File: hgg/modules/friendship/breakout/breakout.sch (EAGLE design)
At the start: 7 parts, among them IC1 MAX481CSA, IC2 MAX481CSA

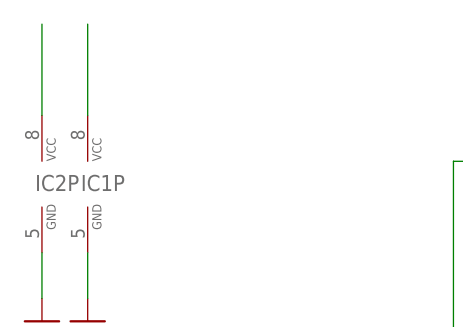
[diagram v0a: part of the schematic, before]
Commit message: max485 now running @ 5V vcc
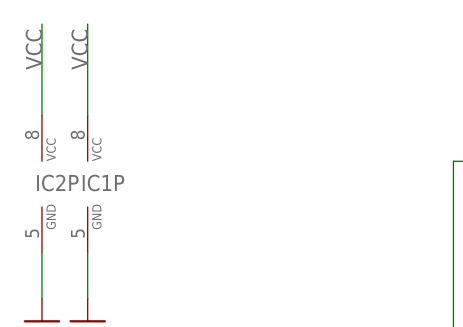
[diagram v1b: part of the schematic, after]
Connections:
- removed net N$18: JP1.3, U$1.+5V_A
- new net 3V3: JP1.7, U$1.+3V3_A
- net VCC: now also JP1.3, U$1.+5V_A; no longer JP1.7, U$1.+3V3_A
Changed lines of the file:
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@@
 <pinref part="IC1" gate="P" pin="VCC"/>
 <wire x1="-76.2" y1="96.52" x2="-76.2" y2="106.68" width="0.1524" layer="91"/>
+<label x="-76.2" y="101.6" size="1.778" layer="95" rot="R90"/>
 </segment>
 <segment>
 <pinref part="IC2" gate="P" pin="VCC"/>
 <wire x1="-81.28" y1="96.52" x2="-81.28" y2="106.68" width="0.1524" layer="91"/>
+<label x="-81.28" y="101.6" size="1.778" layer="95" rot="R90"/>
 </segment>
 <segment>
-<pinref part="U$1" gate="G$1" pin="+3V3_A"/>
-<wire x1="50.8" y1="68.58" x2="50.8" y2="71.12" width="0.1524" layer="91"/>
-<pinref part="JP1" gate="A" pin="7"/>
-<wire x1="50.8" y1="71.12" x2="35.56" y2="71.12" width="0.1524" layer="91"/>
+<pinref part="U$1" gate="G$1" pin="+5V_A"/>
+<wire x1="50.8" y1="63.5" x2="40.64" y2="63.5" width="0.1524" layer="91"/>
+<wire x1="40.64" y1="63.5" x2="40.64" y2="60.96" width="0.1524" layer="91"/>
+<pinref part="JP1" gate="A" pin="3"/>
+<wire x1="40.64" y1="60.96" x2="35.56" y2="60.96" width="0.1524" layer="91"/>
 </segment>
 </net>
@@
 <pinref part="JP1" gate="A" pin="5"/>
 <wire x1="35.56" y1="66.04" x2="43.18" y2="66.04" width="0.1524" layer="91"/>
-</segment>
-</net>
-<net name="N$18" class="0">
-<segment>
-<pinref part="U$1" gate="G$1" pin="+5V_A"/>
-<wire x1="50.8" y1="63.5" x2="40.64" y2="63.5" width="0.1524" layer="91"/>
-<wire x1="40.64" y1="63.5" x2="40.64" y2="60.96" width="0.1524" layer="91"/>
-<pinref part="JP1" gate="A" pin="3"/>
-<wire x1="40.64" y1="60.96" x2="35.56" y2="60.96" width="0.1524" layer="91"/>
 </segment>
 </net>
@@
 </segment>
 </net>
+<net name="3V3" class="0">
+<segment>
+<pinref part="U$1" gate="G$1" pin="+3V3_A"/>
+<wire x1="50.8" y1="68.58" x2="50.8" y2="71.12" width="0.1524" layer="91"/>
+<pinref part="JP1" gate="A" pin="7"/>
+<wire x1="50.8" y1="71.12" x2="35.56" y2="71.12" width="0.1524" layer="91"/>
+</segment>
+</net>

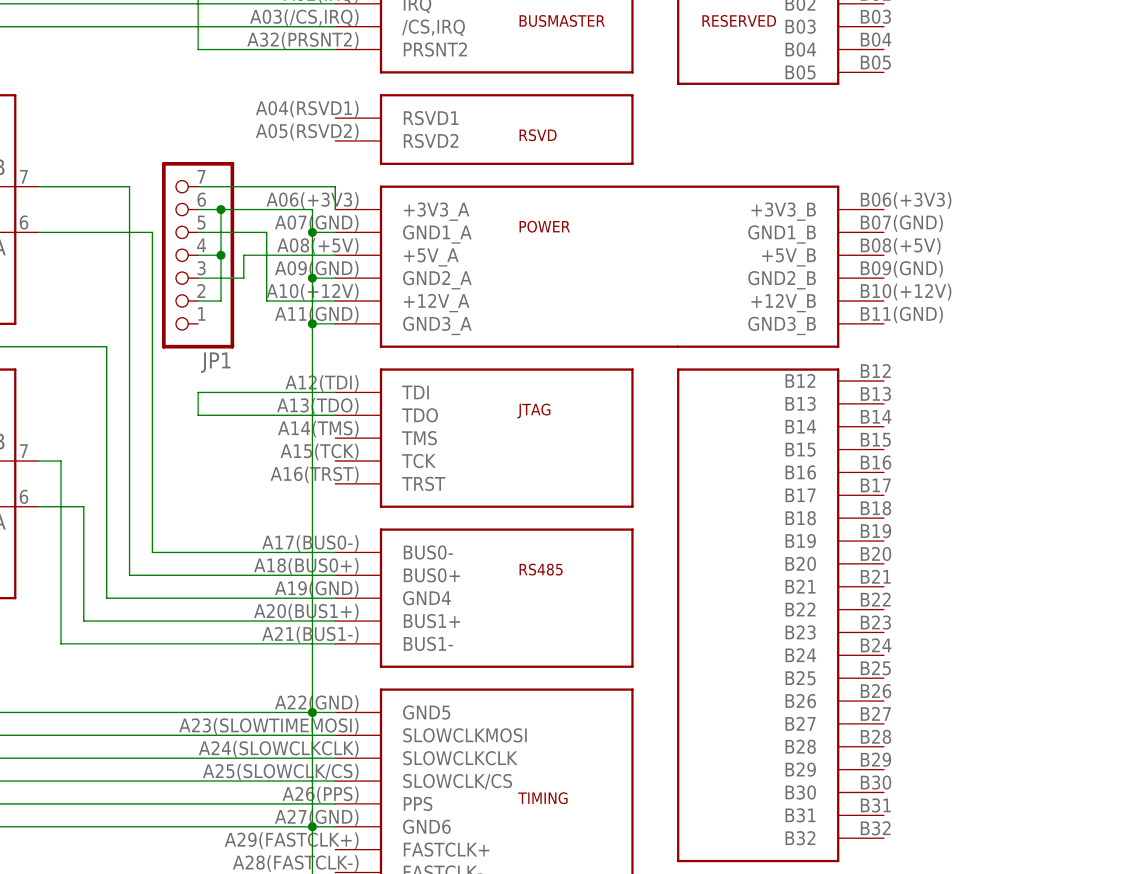
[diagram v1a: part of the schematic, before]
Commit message: swapped sides of the pcb
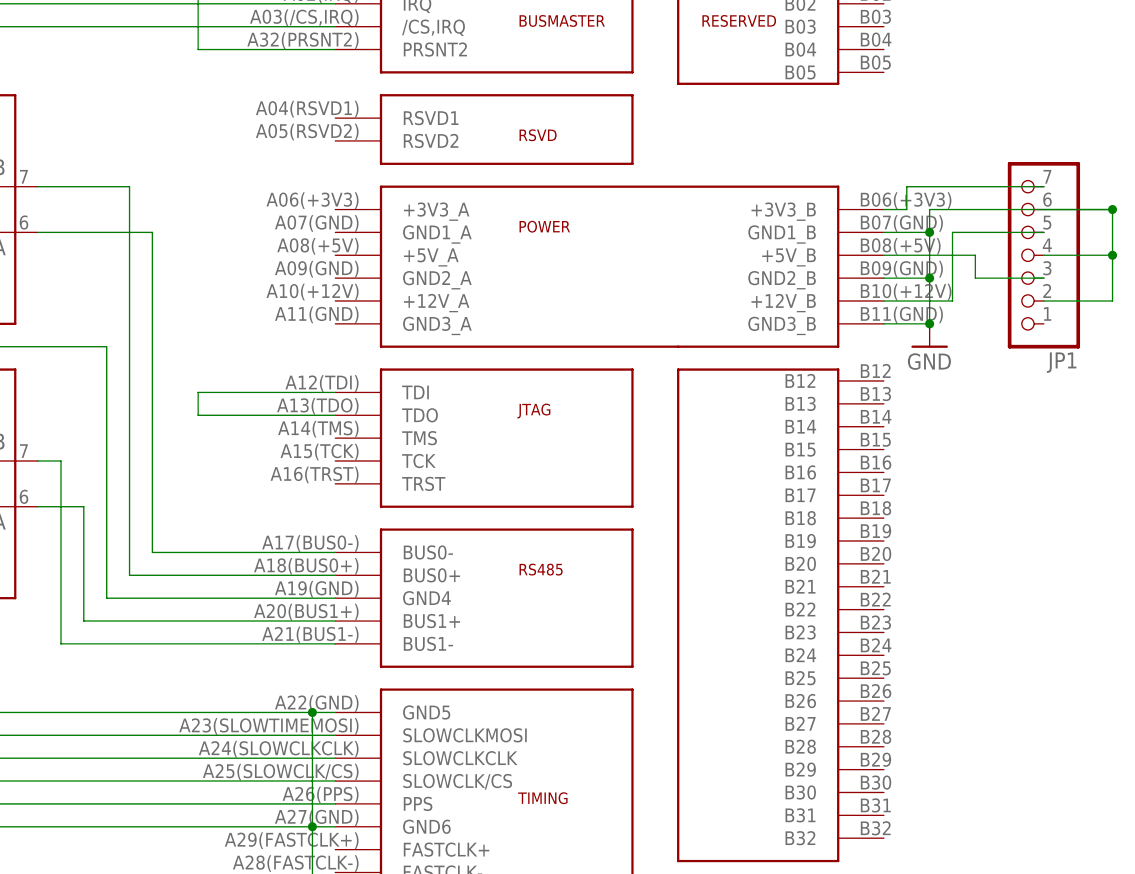
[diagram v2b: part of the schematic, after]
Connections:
- removed net N$13: JP1.5, U$1.+12V_A
- new net 12V: JP1.5, U$1.+12V_B
- net 3V3: now also U$1.+3V3_B; no longer U$1.+3V3_A
- net GND: now also U$1.GND1_B, U$1.GND2_B, U$1.GND3_B; no longer U$1.GND1_A, U$1.GND2_A, U$1.GND3_A
- net VCC: no longer U$1.+5V_A
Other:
- moved on the sheet: JP1
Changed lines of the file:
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@@
 <part name="JP3" library="pinhead" deviceset="PINHD-1X10" device=""/>
 <part name="JP4" library="pinhead" deviceset="PINHD-2X5" device=""/>
+<part name="GND4" library="supply1" deviceset="GND" device=""/>
 </parts>
 <sheets>
@@
 <instance part="IC1" gate="G$1" x="5.08" y="38.1"/>
 <instance part="IC2" gate="G$1" x="5.08" y="68.58"/>
-<instance part="JP1" gate="A" x="33.02" y="63.5" rot="R180"/>
+<instance part="JP1" gate="A" x="127" y="63.5" rot="R180"/>
 <instance part="JP2" gate="A" x="-50.8" y="40.64" rot="R180"/>
 <instance part="IC2" gate="P" x="-81.28" y="88.9"/>
@@
 <instance part="JP3" gate="A" x="40.64" y="-50.8" rot="R180"/>
 <instance part="JP4" gate="A" x="73.66" y="-43.18"/>
+<instance part="GND4" gate="1" x="116.84" y="53.34"/>
 </instances>
 <busses>
@@
 <wire x1="-30.48" y1="25.4" x2="-48.26" y2="25.4" width="0.1524" layer="91"/>
 <junction x="48.26" y="0"/>
-<pinref part="U$1" gate="G$1" pin="GND1_A"/>
-<wire x1="48.26" y1="66.04" x2="50.8" y2="66.04" width="0.1524" layer="91"/>
-<wire x1="48.26" y1="66.04" x2="48.26" y2="60.96" width="0.1524" layer="91"/>
 <pinref part="JP2" gate="A" pin="2"/>
 <pinref part="JP2" gate="A" pin="7"/>
-<pinref part="U$1" gate="G$1" pin="GND2_A"/>
-<wire x1="48.26" y1="60.96" x2="48.26" y2="55.88" width="0.1524" layer="91"/>
-<wire x1="48.26" y1="55.88" x2="48.26" y2="12.7" width="0.1524" layer="91"/>
-<wire x1="50.8" y1="60.96" x2="48.26" y2="60.96" width="0.1524" layer="91"/>
-<junction x="48.26" y="60.96"/>
-<pinref part="U$1" gate="G$1" pin="GND3_A"/>
-<wire x1="50.8" y1="55.88" x2="48.26" y2="55.88" width="0.1524" layer="91"/>
-<junction x="48.26" y="55.88"/>
-<wire x1="48.26" y1="66.04" x2="48.26" y2="68.58" width="0.1524" layer="91"/>
-<junction x="48.26" y="66.04"/>
-<pinref part="JP1" gate="A" pin="2"/>
-<wire x1="35.56" y1="58.42" x2="38.1" y2="58.42" width="0.1524" layer="91"/>
-<wire x1="38.1" y1="58.42" x2="38.1" y2="63.5" width="0.1524" layer="91"/>
-<pinref part="JP1" gate="A" pin="4"/>
-<wire x1="38.1" y1="63.5" x2="35.56" y2="63.5" width="0.1524" layer="91"/>
-<wire x1="38.1" y1="63.5" x2="38.1" y2="68.58" width="0.1524" layer="91"/>
-<junction x="38.1" y="63.5"/>
-<pinref part="JP1" gate="A" pin="6"/>
-<wire x1="38.1" y1="68.58" x2="35.56" y2="68.58" width="0.1524" layer="91"/>
-<wire x1="38.1" y1="68.58" x2="48.26" y2="68.58" width="0.1524" layer="91"/>
-<junction x="38.1" y="68.58"/>
 </segment>
 <segment>
@@
 <pinref part="GND3" gate="1" pin="GND"/>
 <wire x1="-76.2" y1="76.2" x2="-76.2" y2="81.28" width="0.1524" layer="91"/>
+</segment>
+<segment>
+<pinref part="JP1" gate="A" pin="6"/>
+<pinref part="JP1" gate="A" pin="4"/>
+<pinref part="JP1" gate="A" pin="2"/>
+<wire x1="129.54" y1="58.42" x2="137.16" y2="58.42" width="0.1524" layer="91"/>
+<wire x1="137.16" y1="58.42" x2="137.16" y2="63.5" width="0.1524" layer="91"/>
+<wire x1="137.16" y1="63.5" x2="129.54" y2="63.5" width="0.1524" layer="91"/>
+<junction x="137.16" y="63.5"/>
+<wire x1="137.16" y1="63.5" x2="137.16" y2="68.58" width="0.1524" layer="91"/>
+<wire x1="137.16" y1="68.58" x2="129.54" y2="68.58" width="0.1524" layer="91"/>
+<junction x="137.16" y="68.58"/>
+<wire x1="137.16" y1="68.58" x2="116.84" y2="68.58" width="0.1524" layer="91"/>
+<wire x1="116.84" y1="68.58" x2="116.84" y2="66.04" width="0.1524" layer="91"/>
+<pinref part="U$1" gate="G$1" pin="GND1_B"/>
+<wire x1="116.84" y1="66.04" x2="111.76" y2="66.04" width="0.1524" layer="91"/>
+<wire x1="116.84" y1="66.04" x2="116.84" y2="60.96" width="0.1524" layer="91"/>
+<junction x="116.84" y="66.04"/>
+<pinref part="U$1" gate="G$1" pin="GND2_B"/>
+<wire x1="116.84" y1="60.96" x2="111.76" y2="60.96" width="0.1524" layer="91"/>
+<wire x1="116.84" y1="60.96" x2="116.84" y2="55.88" width="0.1524" layer="91"/>
+<junction x="116.84" y="60.96"/>
+<pinref part="U$1" gate="G$1" pin="GND3_B"/>
+<wire x1="116.84" y1="55.88" x2="111.76" y2="55.88" width="0.1524" layer="91"/>
+<pinref part="GND4" gate="1" pin="GND"/>
+<junction x="116.84" y="55.88"/>
 </segment>
 </net>
@@
 </segment>
 <segment>
-<pinref part="U$1" gate="G$1" pin="+5V_A"/>
-<wire x1="50.8" y1="63.5" x2="40.64" y2="63.5" width="0.1524" layer="91"/>
-<wire x1="40.64" y1="63.5" x2="40.64" y2="60.96" width="0.1524" layer="91"/>
+<wire x1="111.76" y1="63.5" x2="121.92" y2="63.5" width="0.1524" layer="91"/>
+<wire x1="121.92" y1="63.5" x2="121.92" y2="60.96" width="0.1524" layer="91"/>
 <pinref part="JP1" gate="A" pin="3"/>
-<wire x1="40.64" y1="60.96" x2="35.56" y2="60.96" width="0.1524" layer="91"/>
+<wire x1="121.92" y1="60.96" x2="129.54" y2="60.96" width="0.1524" layer="91"/>
 </segment>
 </net>
@@
 </segment>
 </net>
-<net name="N$13" class="0">
-<segment>
-<pinref part="U$1" gate="G$1" pin="+12V_A"/>
-<wire x1="50.8" y1="58.42" x2="43.18" y2="58.42" width="0.1524" layer="91"/>
-<wire x1="43.18" y1="58.42" x2="43.18" y2="66.04" width="0.1524" layer="91"/>
+<net name="12V" class="0">
+<segment>
+<wire x1="119.38" y1="58.42" x2="119.38" y2="66.04" width="0.1524" layer="91"/>
 <pinref part="JP1" gate="A" pin="5"/>
-<wire x1="35.56" y1="66.04" x2="43.18" y2="66.04" width="0.1524" layer="91"/>
+<wire x1="129.54" y1="66.04" x2="119.38" y2="66.04" width="0.1524" layer="91"/>
+<pinref part="U$1" gate="G$1" pin="+12V_B"/>
+<wire x1="119.38" y1="58.42" x2="111.76" y2="58.42" width="0.1524" layer="91"/>
 </segment>
 </net>
@@
 <net name="3V3" class="0">
 <segment>
-<pinref part="U$1" gate="G$1" pin="+3V3_A"/>
-<wire x1="50.8" y1="68.58" x2="50.8" y2="71.12" width="0.1524" layer="91"/>
 <pinref part="JP1" gate="A" pin="7"/>
-<wire x1="50.8" y1="71.12" x2="35.56" y2="71.12" width="0.1524" layer="91"/>
-</segment>
-</net>
+<wire x1="114.3" y1="71.12" x2="129.54" y2="71.12" width="0.1524" layer="91"/>
+<pinref part="U$1" gate="G$1" pin="+3V3_B"/>
+<wire x1="111.76" y1="68.58" x2="114.3" y2="68.58" width="0.1524" layer="91"/>
+<wire x1="114.3" y1="68.58" x2="114.3" y2="71.12" width="0.1524" layer="91"/>
+</segment>
+</net>

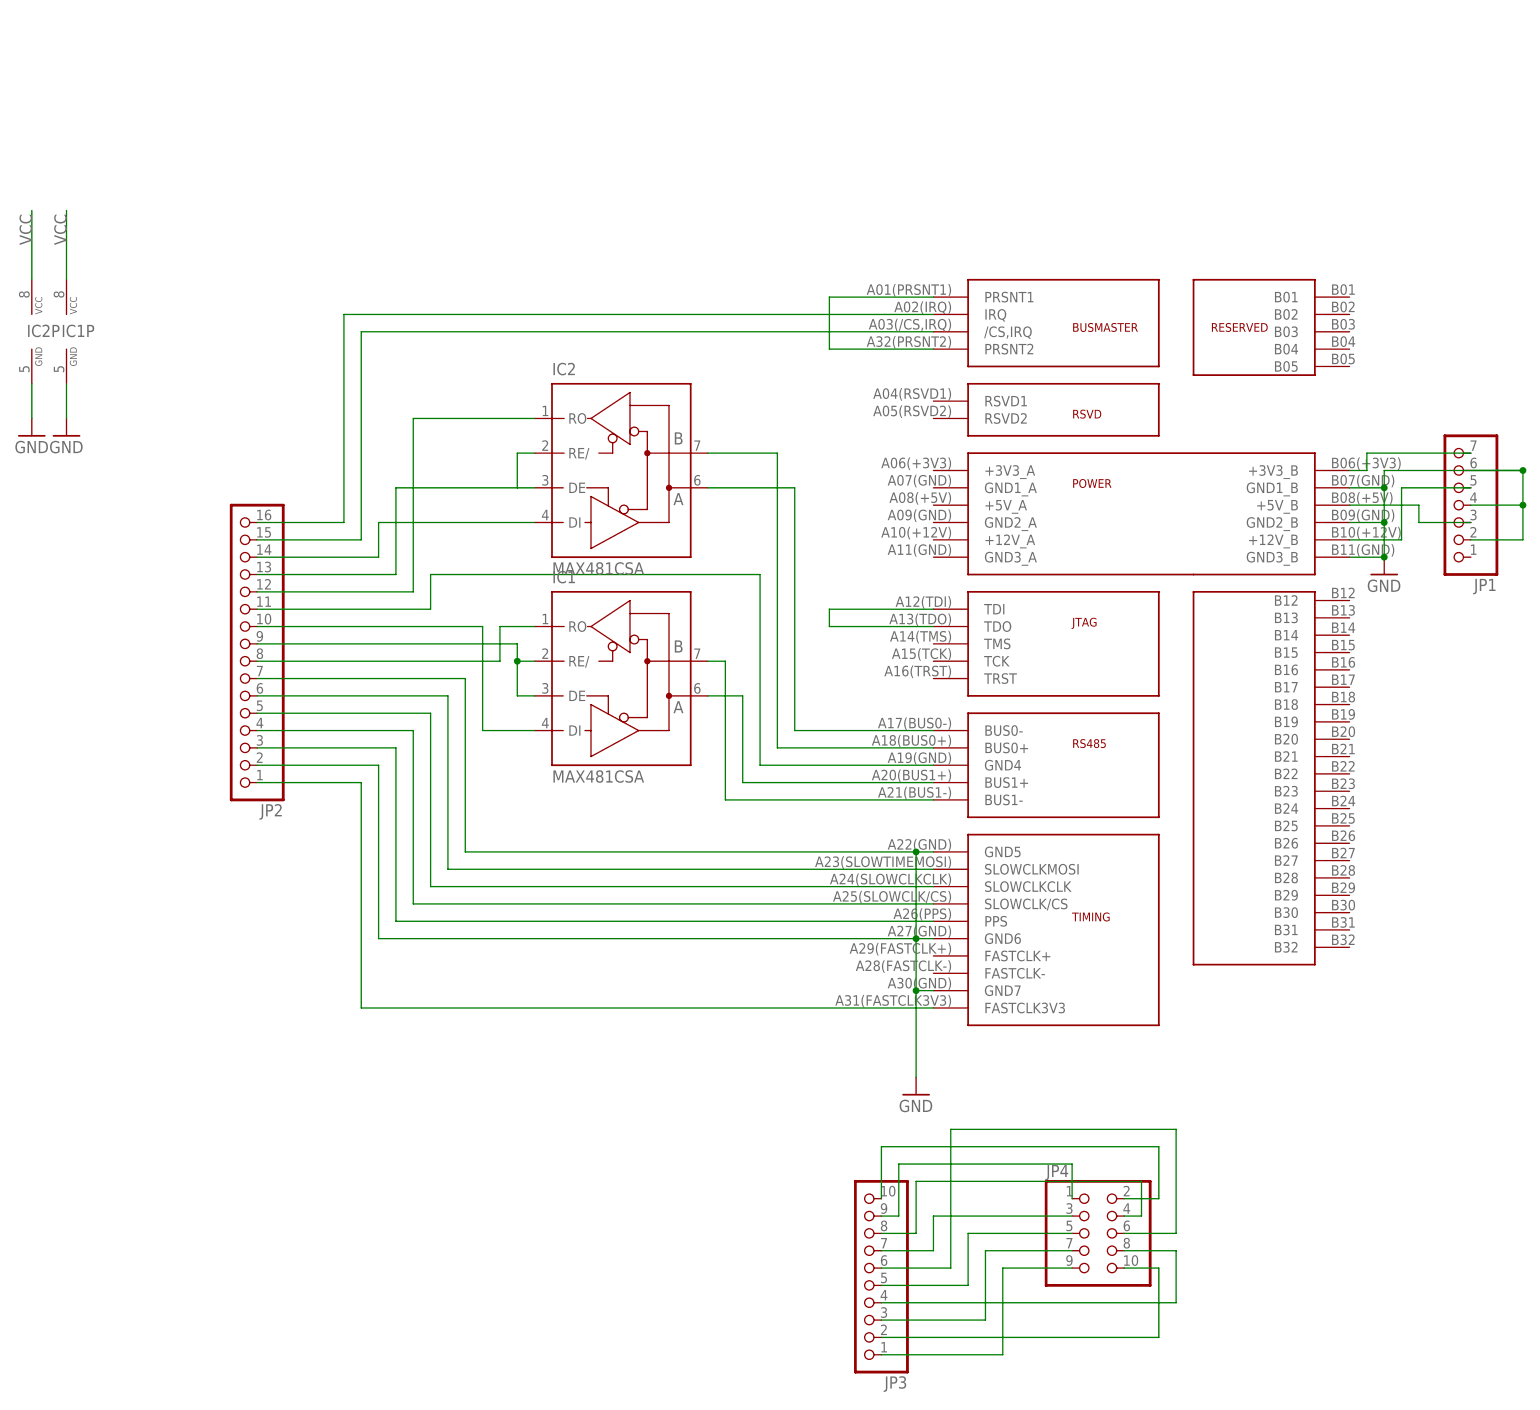
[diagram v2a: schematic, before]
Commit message: changed breakout to use full busmaster plug port
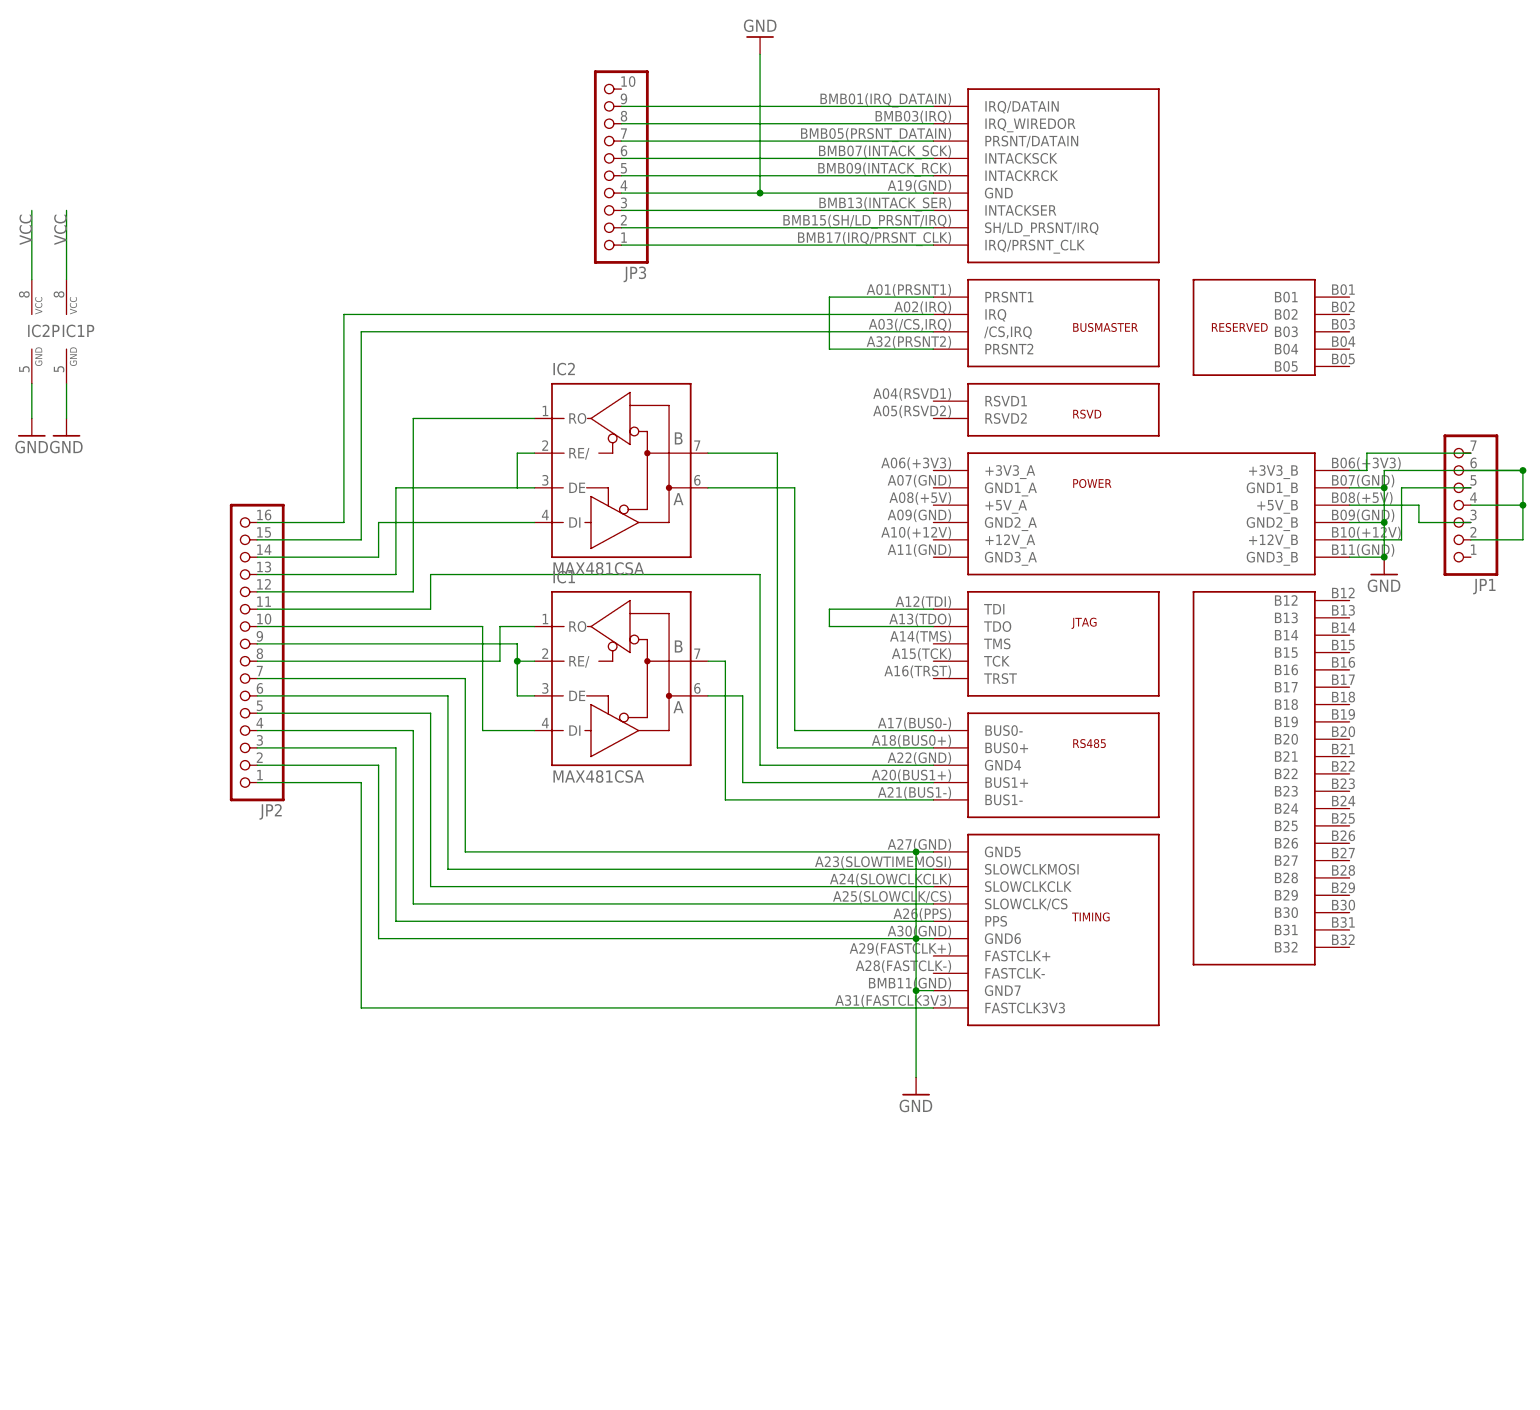
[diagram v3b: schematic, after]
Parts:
- removed JP4: (no value), pinhead:PINHD-2X5
- U$1: value FRIENDSHIPCONNECTOR -> BUSMASTER; device hgg:FRIENDSHIPCONNECTOR -> hgg:BUSMASTER
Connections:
- removed net N$24: JP3.9, JP4.1
- removed net N$30: JP3.4, JP4.8
- removed net N$31: JP3.2, JP4.10
- removed net N$32: JP3.1, JP4.9
- new net N$13: JP3.1, U$1.IRQ/PRSNT_CLK
- new net N$18: JP3.2, U$1.SH/LD_PRSNT/IRQ
- net GND: now also JP3.4, U$1.GND
- net N$22: now also JP3.3, U$1.INTACKSER; no longer JP3.10, JP4.2
- net N$25: now also JP3.5, U$1.INTACKRCK; no longer JP3.8, JP4.4
- net N$26: now also JP3.6, U$1.INTACKSCK; no longer JP3.7, JP4.3
- net N$27: now also JP3.7, U$1.PRSNT/DATAIN; no longer JP3.6, JP4.6
- net N$28: now also JP3.8, U$1.IRQ_WIREDOR; no longer JP3.5, JP4.5
- net N$29: now also JP3.9, U$1.IRQ/DATAIN; no longer JP3.3, JP4.7
- net VCC: now also U$1.+5V_B
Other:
- moved on the sheet: JP3
